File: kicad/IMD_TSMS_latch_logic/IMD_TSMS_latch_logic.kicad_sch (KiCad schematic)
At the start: 23 parts, among them IC1 NE555, Q1 PMOS, Q2 PMOS, SW1 SW_Push, U1 4001, U2 4009, U3 4009, U4 4001

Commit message: latch ahhhh
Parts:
- removed Q1, Q2: PMOS, symbol Simulation_SPICE:PMOS
- added C4, C5, C6, C7, C9: 100nF, RMC_Capacitor:C_0805_2012Metric_Pad1.18x1.45mm_HandSolder_L, symbol Device:C
- added J1, J2, J3, J4: Conn_01x02, symbol Connector_Generic:Conn_01x02
- added K1: SANYOU_SRD_Form_C, Relay_THT:Relay_SPDT_SANYOU_SRD_Series_Form_C, symbol Relay:SANYOU_SRD_Form_C
- added Q1, Q2, Q3: Q_PMOS_GDS, RMC_TO:TO-252-2, symbol Transistor_FET:Q_PMOS_GDS
- added R10, R9: 100k, RMC_Resistor:R_0805_2012Metric_Pad1.20x1.40mm_HandSolder_L, symbol Device:R
- added R11, R12: 2k2, RMC_Resistor:R_0805_2012Metric_Pad1.20x1.40mm_HandSolder_L, symbol Device:R
- C1, C2, C3: footprint (none) -> RMC_Capacitor:C_0805_2012Metric_Pad1.18x1.45mm_HandSolder_L
- D1: footprint (none) -> Diode_SMD:D_SMA_Handsoldering
- IC1: footprint SOIC127P600X175-8N -> RMC_SO:SOIC-8_3.9x4.9mm_P1.27mm_RMC_Handsolder
- R1, R2, R3, R4, R5, R6, R7, R8: footprint (none) -> RMC_Resistor:R_0805_2012Metric_Pad1.20x1.40mm_HandSolder_L
- SW1: footprint (none) -> Connector_JST:JST_XH_B2B-XH-A_1x02_P2.50mm_Vertical
- U1: footprint (none) -> RMC_SO:SOIC127P600X175-14N
- U2, U3: footprint (none) -> RMC_SO:SOIC-16_3.9x9.9mm_P1.27mm_Handsolder
- U4: footprint (none) -> RMC_SO:TSSOP-20_4.4x6.5mm_P0.65mm
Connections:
- net +12V: now also C4.1, C5.1, C6.1, C7.1, C9.1, J4.1 (Pin_1), Q1.3 (S), Q2.3 (S), Q3.3 (S)
- net GND: now also C4.2, C5.2, C6.2, C7.2, C9.2, J2.2 (Pin_2), J4.2 (Pin_2), K1.5, R10.2, R11.2, R12.2, R9.2
- net IMD_OKHs: now also J1.2 (Pin_2), R11.1
- net IMD_reset: now also Q3.2 (D)
- net fall_edge_out: now also Q3.1 (G), R9.1
- net at R4.2: now also Q2.1 (G), R10.1
- net at C2.1, R2.1: now also Q2.2 (D)
- net IMD_latch_output renamed IMD_RELAY
- net IMD_RELAY: now also K1.2, Q1.1 (G)
- new net IMD_LED: J2.1 (Pin_1), Q1.2 (D)
- new net IMD_MHs: J1.1 (Pin_1), R12.1
- new net SDC_IN: J3.1 (Pin_1), K1.1
- new net SDC_OUT: J3.2 (Pin_2), K1.4
- no-connect marks 22 -> 23
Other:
- note added: "IMD latch connectors"
- moved on the sheet: C1, IC1, R7, R8, U2G

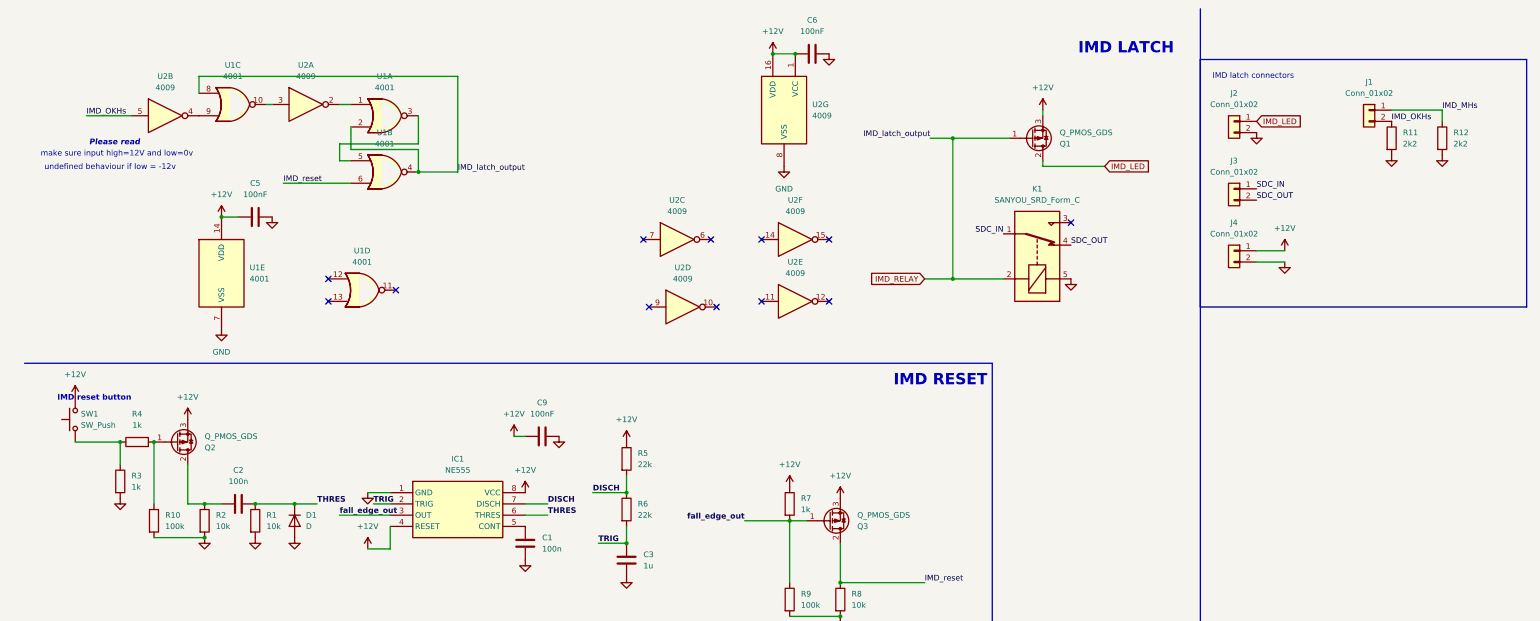
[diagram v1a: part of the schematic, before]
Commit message: Draw IMD latch
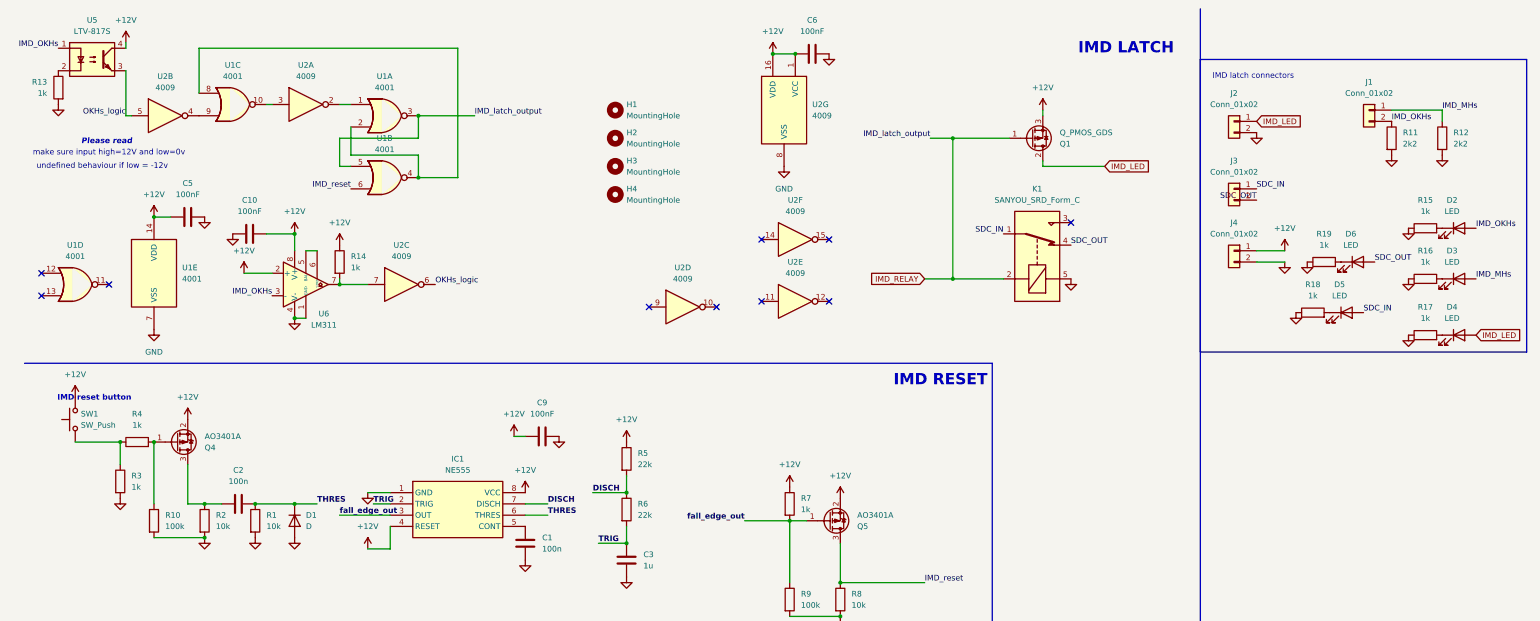
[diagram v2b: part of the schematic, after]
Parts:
- removed Q2, Q3: Q_PMOS_GDS, RMC_TO:TO-252-2, symbol Transistor_FET:Q_PMOS_GDS
- added C10: 100nF, RMC_Capacitor:C_0805_2012Metric_Pad1.18x1.45mm_HandSolder_L, symbol Device:C
- added D2, D3, D4, D5, D6: LED, RMC_LED:LED_0805_2012Metric_Pad1.45x1.40mm_HandSolder, symbol Device:LED
- added H1, H2, H3, H4: MountingHole, MountingHole:MountingHole_4.3mm_M4, symbol Mechanical:MountingHole
- added Q4, Q5: AO3401A, RMC_SOT:SOT-23, symbol Transistor_FET:AO3401A
- added R13, R14, R15, R16, R17, R18, R19: 1k, RMC_Resistor:R_0805_2012Metric_Pad1.20x1.40mm_HandSolder_L, symbol Device:R
- added U5: LTV-817S, Package_DIP:SMDIP-4_W9.53mm, symbol Isolator:LTV-817S
- added U6: LM311, RMC_SO:SOIC-8_3.9x4.9mm_P1.27mm_RMC_Handsolder, symbol Comparator:LM311
- J1, J2, J3, J4: footprint (none) -> Connector_Molex:Molex_Micro-Fit_3.0_43650-0215_1x02_P3.00mm_Vertical
- SW1: footprint Connector_JST:JST_XH_B2B-XH-A_1x02_P2.50mm_Vertical -> Connector_Molex:Molex_Micro-Fit_3.0_43650-0215_1x02_P3.00mm_Vertical
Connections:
- net +12V: now also C10.1, Q4.2 (S), Q5.2 (S), R14.1, U5.4, U6.2 (+), U6.8 (V+)
- net GND: now also C10.2, R13.2, R15.1, R16.1, R17.1, R18.1, R19.1, U6.1 (GND), U6.4 (V-)
- net IMD_LED: now also D4.2 (A)
- net IMD_MHs: now also D3.2 (A)
- net IMD_OKHs: now also D2.2 (A), U5.1, U6.3 (-); no longer U2.5
- net IMD_RELAY: now also U1.3, U1.5; no longer U1.2, U1.4, U1.8
- net IMD_reset: now also Q5.3 (D)
- net SDC_IN: now also D5.2 (A)
- net SDC_OUT: now also D6.2 (A)
- net fall_edge_out: now also Q5.1 (G)
- net at R10.1, R4.2: now also Q4.1 (G)
- net at C2.1, R2.1: now also Q4.3 (D)
- net OKHs_logic: now reaches U2.6
- net OKHs_logic: now also U2.5, U5.3
- net at U2.7: now also R14.2, U6.7
- new net: D4.1 (K), R17.2
- new net: D3.1 (K), R16.2
- new net: D6.1 (K), R19.2
- new net: U6.5 (BAL), U6.6 (STRB)
- new net: R13.1, U5.2
- new net: D2.1 (K), R15.2
- new net: D5.1 (K), R18.2
- new net: U1.2, U1.4, U1.8
- no-connect marks 23 -> 21
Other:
- moved on the sheet: C5, U1B, U1D, U1E

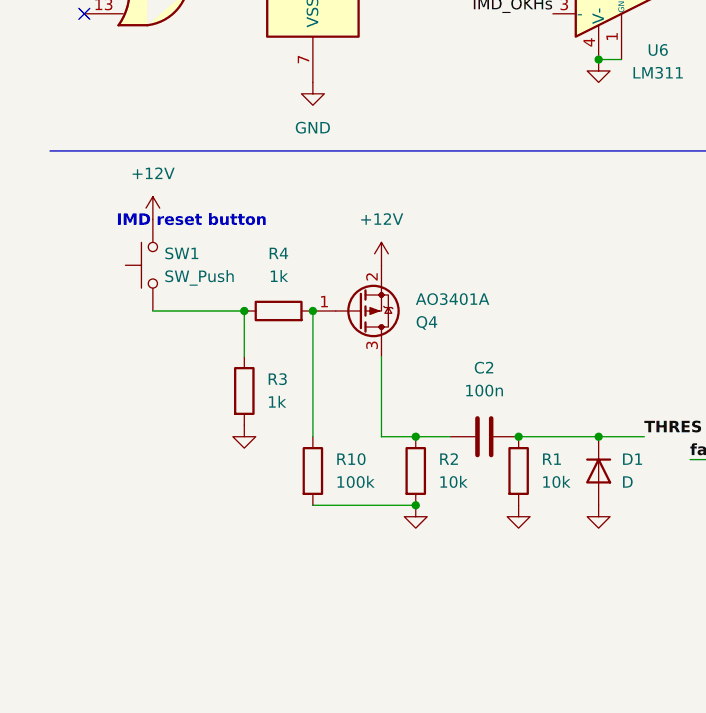
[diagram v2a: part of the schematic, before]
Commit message: IMD latch with small IMD moutning
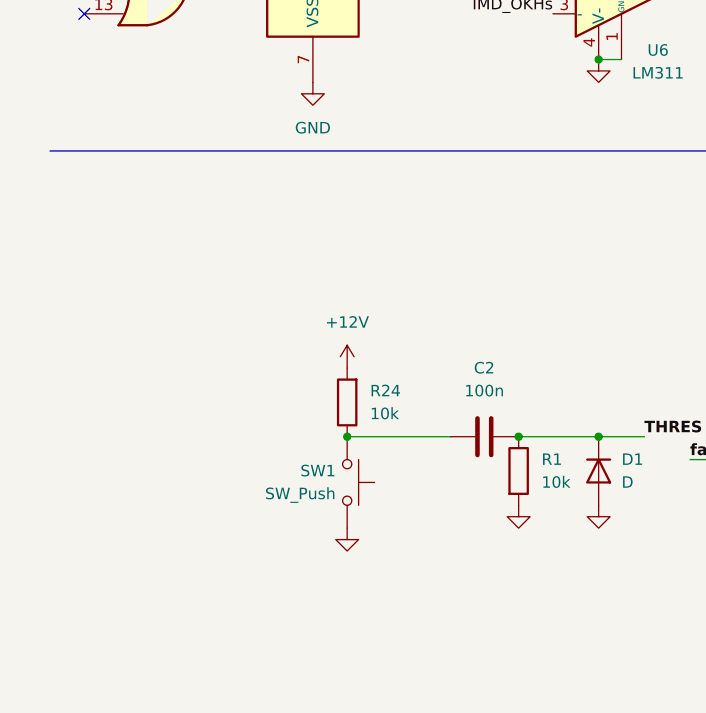
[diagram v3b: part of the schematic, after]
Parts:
- removed Q4: AO3401A, RMC_SOT:SOT-23, symbol Transistor_FET:AO3401A
- removed R10: 100k, RMC_Resistor:R_0805_2012Metric_Pad1.20x1.40mm_HandSolder_L, symbol Device:R
- removed R2: 10k, RMC_Resistor:R_0805_2012Metric_Pad1.20x1.40mm_HandSolder_L, symbol Device:R
- removed R3, R4: 1k, RMC_Resistor:R_0805_2012Metric_Pad1.20x1.40mm_HandSolder_L, symbol Device:R
- added R24: 10k, RMC_Resistor:R_0805_2012Metric_Pad1.20x1.40mm_HandSolder_L, symbol Device:R
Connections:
- net +12V: now also R24.2; no longer SW1.2
- net GND: now also SW1.1
- net at C2.1: now also SW1.2, R24.1
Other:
- note removed: "IMD reset button"
- moved on the sheet: SW1

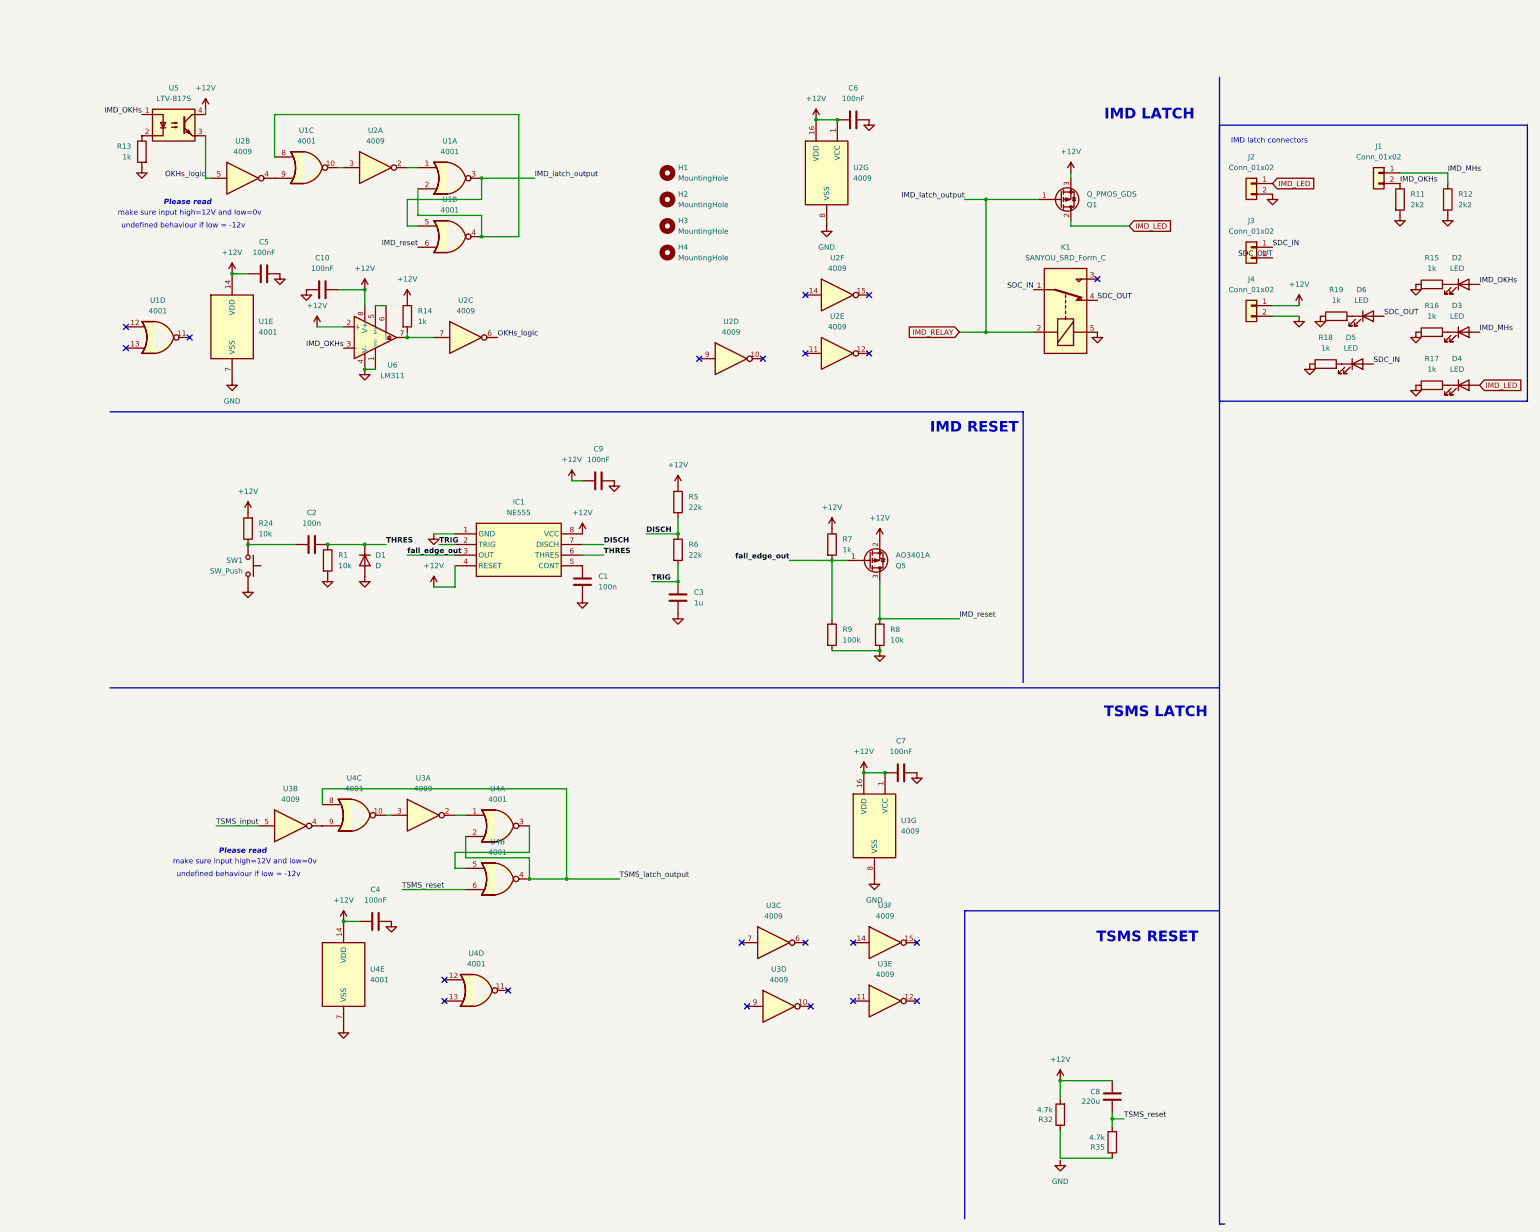
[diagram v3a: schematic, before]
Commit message: imd latch and LED pull high
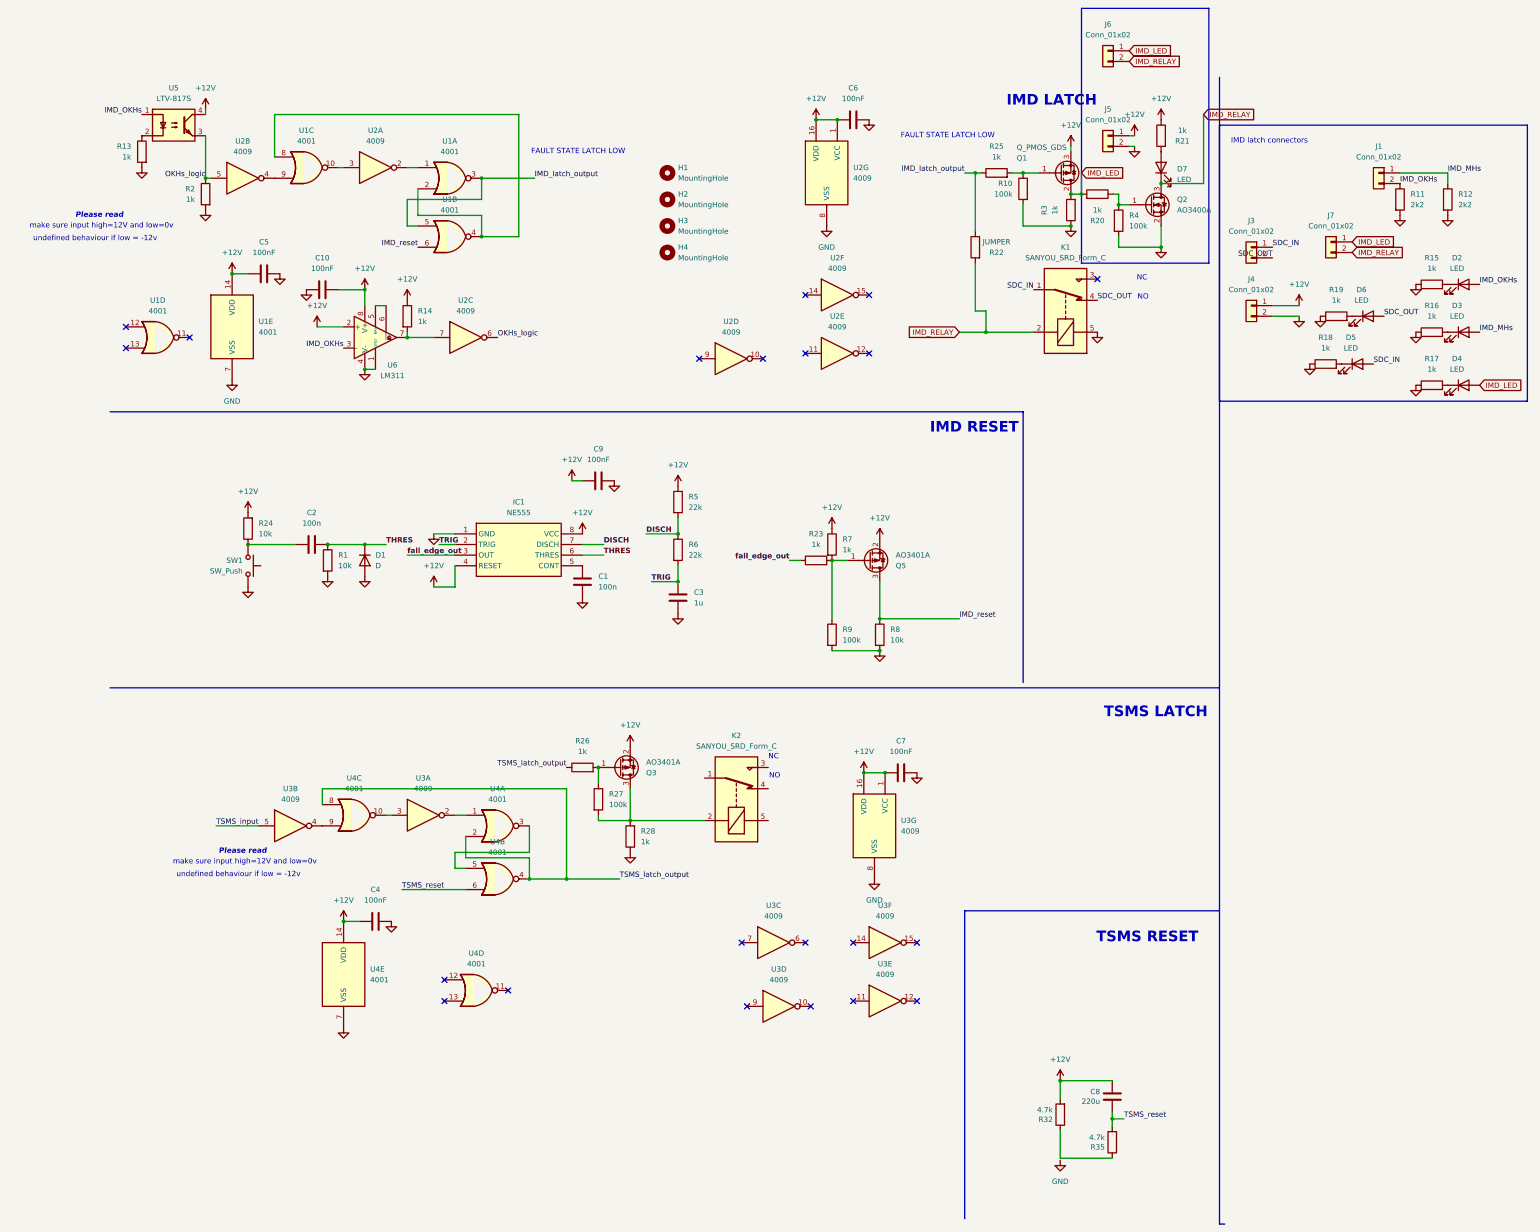
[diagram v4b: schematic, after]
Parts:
- removed J2: Conn_01x02, Connector_Molex:Molex_Micro-Fit_3.0_43650-0215_1x02_P3.00mm_Vertical, symbol Connector_Generic:Conn_01x02
- added D7: LED, RMC_LED:LED_0805_2012Metric_Pad1.45x1.40mm_HandSolder, symbol Device:LED
- added J5, J6, J7: Conn_01x02, Connector_Molex:Molex_Micro-Fit_3.0_43650-0215_1x02_P3.00mm_Vertical, symbol Connector_Generic:Conn_01x02
- added K2: SANYOU_SRD_Form_C, Relay_THT:Relay_SPDT_SANYOU_SRD_Series_Form_C, symbol Relay:SANYOU_SRD_Form_C
- added Q2: AO3400A, Package_TO_SOT_SMD:SOT-23, symbol Transistor_FET:AO3400A
- added Q3: AO3401A, RMC_SOT:SOT-23, symbol Transistor_FET:AO3401A
- added R10, R27, R4: 100k, RMC_Resistor:R_0805_2012Metric_Pad1.20x1.40mm_HandSolder_L, symbol Device:R
- added R2, R20, R21, R23, R25, R26, R28, R3: 1k, RMC_Resistor:R_0805_2012Metric_Pad1.20x1.40mm_HandSolder_L, symbol Device:R
- added R22: JUMPER, RMC_Resistor:R_0805_2012Metric_Pad1.20x1.40mm_HandSolder_L, symbol Device:R
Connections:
- net +12V: now also J5.1 (Pin_1), Q3.2 (S), R21.1
- net GND: now also J5.2 (Pin_2), Q2.2 (S), R10.2, R2.2, R28.1, R3.1, R4.2
- net IMD_LED: now also J6.1 (Pin_1), J7.1 (Pin_1), R20.2, R3.2
- net IMD_RELAY: now also D7.1 (K), J6.2 (Pin_2), J7.2 (Pin_2), Q2.3 (D), R22.2; no longer Q1.1 (G), U1.3, U1.5
- net OKHs_logic: now also R2.1
- net TSMS_latch_output: now also R26.1
- net fall_edge_out: now also R23.1; no longer Q5.1 (G), R7.2, R9.1
- new net: Q2.1 (G), R20.1, R4.1
- new net: D7.2 (A), R21.2
- new net: Q3.1 (G), R26.2, R27.1
- new net: K2.2, Q3.3 (D), R27.2, R28.2
- new net: Q5.1 (G), R23.2, R7.2, R9.1
- new net: Q1.1 (G), R10.1, R25.2
- new net IMD_latch_output: R22.1, R25.1, U1.3, U1.5
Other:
- note added: "FAULT STATE LATCH LOW"
- note added: "NC"
- note added: "NO"
- moved on the sheet: Q1

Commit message: did all 3 boards
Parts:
- removed Q1: Q_PMOS_GDS, RMC_TO:TO-252-2, symbol Transistor_FET:Q_PMOS_GDS
- added H10, H11, H12, H5, H6, H7, H8, H9: MountingHole, MountingHole:MountingHole_4.3mm_M4, symbol Mechanical:MountingHole
- added J8, J9: Conn_01x02, Connector_Molex:Molex_Micro-Fit_3.0_43650-0215_1x02_P3.00mm_Vertical, symbol Connector_Generic:Conn_01x02
- added Q6: AO3401A, RMC_SOT:SOT-23, symbol Transistor_FET:AO3401A
- C8: footprint RMC_Capacitor:C_0805_2012Metric_Pad1.18x1.45mm_HandSolder_L -> RMC_Capacitor:CP_Radial_D6.3mm_P2.50mm_extended
- Q2: footprint Package_TO_SOT_SMD:SOT-23 -> RMC_SOT:SOT-23
- U4: footprint RMC_SO:TSSOP-20_4.4x6.5mm_P0.65mm -> RMC_SO:SOIC127P600X175-14N
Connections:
- net +12V: now also J8.1 (Pin_1), Q6.2 (S)
- net GND: now also K2.5, J8.2 (Pin_2)
- net IMD_LED: now also J6.2 (Pin_2), Q6.3 (D); no longer J6.1 (Pin_1)
- net IMD_RELAY: now also J6.1 (Pin_1); no longer J6.2 (Pin_2)
- net TSMS_input: now also K2.1, J9.1 (Pin_1)
- net at R10.1, R25.2: now also Q6.1 (G)
- net TSMS_output: now reaches K2.4
- net TSMS_output: now also J9.2 (Pin_2)
- no-connect marks 21 -> 22
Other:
- moved on the sheet: J5
